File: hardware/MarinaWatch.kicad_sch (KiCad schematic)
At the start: 18 parts, among them J1 USB_C_Receptacle_USB2.0_16P, J2 Screw_Terminal_01x02, U1 ESP32-S3-MINI-1, U2 MCP73831-2-OT, U3 AP2112K-3.3

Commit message: Working on analog sensor
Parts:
- added Q101: PMOS, symbol Simulation_SPICE:PMOS
- added R101, R103: 110R, Resistor_SMD:R_0603_1608Metric_Pad0.98x0.95mm_HandSolder, symbol Device:R
- added R102: 100R, Resistor_SMD:R_0603_1608Metric_Pad0.98x0.95mm_HandSolder, symbol Device:R
- added TH101: 100R, symbol Device:Thermistor_PTC
- added TP101, TP102, TP103, TP104: TestPoint, symbol Connector:TestPoint
- added U101, U102, U103: ${SIM.PARAMS}, symbol Simulation_SPICE:OPAMP
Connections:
- net +3V3: now also R101.1, R103.1, U101.3 (V+), U102.3 (V+), U103.3 (V+)
- net GND: now also R102.2, TH101.2, U101.4 (V-), U102.4 (V-), U103.4 (V-)
- new net PT_ANALOG: R103.2, TH101.1, TP101.1, U101.1 (+)
- new net PT_DIFF_N: TP104.1, U102.2 (-), U102.5, U103.2 (-)
- new net PT_DIFF_P: TP103.1, U101.2 (-), U101.5, U103.1 (+)
- new net PT_REF: R101.2, R102.1, TP102.1, U102.1 (+)

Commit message: Working on production version
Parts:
- removed D1, D2, D3: 1N5819, Diode_SMD:D_SOD-123, symbol Diode:1N5819
- removed J2: Screw_Terminal_01x02, TerminalBlock_MetzConnect:TerminalBlock_MetzConnect_Type101_RT01602HBWC_1x02_P5.08mm_Horizontal, symbol Connector:Screw_Terminal_01x02
- removed Q101: PMOS, symbol Simulation_SPICE:PMOS
- removed R101, R103: 110R, Resistor_SMD:R_0603_1608Metric_Pad0.98x0.95mm_HandSolder, symbol Device:R
- removed R102: 100R, Resistor_SMD:R_0603_1608Metric_Pad0.98x0.95mm_HandSolder, symbol Device:R
- removed TH101: 100R, symbol Device:Thermistor_PTC
- removed TP101, TP102, TP103, TP104: TestPoint, symbol Connector:TestPoint
- removed U101, U102, U103: ${SIM.PARAMS}, symbol Simulation_SPICE:OPAMP
- removed U2: MCP73831-2-OT, Package_TO_SOT_SMD:SOT-23-5, symbol Battery_Management:MCP73831-2-OT
- removed U3: AP2112K-3.3, Package_TO_SOT_SMD:SOT-23-5, symbol Regulator_Linear:AP2112K-3.3
- added BT1, BT2: Battery_Cell, symbol Device:Battery_Cell
- added C3, C6: 10u, Capacitor_SMD:C_0603_1608Metric_Pad1.08x0.95mm_HandSolder, symbol Device:C
- added C4, C7, C8: 22u, Capacitor_SMD:C_0603_1608Metric_Pad1.08x0.95mm_HandSolder, symbol Device:C
- added C5: 100n, Capacitor_SMD:C_0603_1608Metric_Pad1.08x0.95mm_HandSolder, symbol Device:C
- added L1: 1u5, symbol Device:L
- added R10, R11, R12, R15, R9: 5k1, Resistor_SMD:R_0603_1608Metric_Pad0.98x0.95mm_HandSolder, symbol Device:R
- added R13: 470k, Resistor_SMD:R_0603_1608Metric_Pad0.98x0.95mm_HandSolder, symbol Device:R
- added R14: 150k, Resistor_SMD:R_0603_1608Metric_Pad0.98x0.95mm_HandSolder, symbol Device:R
- added TH1, TH2: Thermistor_NTC, symbol Device:Thermistor_NTC
- added U2, U4: BQ24210, symbol KiCAD-LIB:BQ24210
- added U5: TPS63070, symbol KiCAD-LIB:TPS63070
- R1, R2: value 12k -> 0R
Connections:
- net +3V3: now also C4.1, C7.1, C8.1, R13.1, U5.7 (VOUT), U5.8 (VOUT); no longer C2.1
- net +BATT: now also C2.1, R1.2, R2.2, BT1.1 (+), BT2.1 (+), C6.1, R15.1, U5.12 (VIN), U5.13 (VIN); no longer R5.1
- net GND: now also R7.2, BT1.2 (-), BT2.2 (-), C3.2, C4.2, C5.2, C6.2, C7.2, C8.2, R10.2, R11.2, R14.2, R9.2, TH1.2, TH2.2, U2.3 (VSS), U4.3 (VSS), U5.10 (PGND), U5.15 (VSEL), U5.4 (GND), U5.6 (FB2); no longer R2.2
- net SOLAR: now also C1.1, U2.1 (VBUS); no longer R7.1
- net VBUS: now also C3.1, U4.1 (VBUS)
- net V_BAT: no longer R5.2, R6.1
- net V_SOLAR: no longer R7.2, R8.1
- net at R2.1: now also U2.10 (BAT)
- net VCC: no longer names the net of R1.1
- net VCC: now also U4.10 (BAT); no longer C1.1
- new net: R12.1, U4.4 (VTSB)
- new net: R12.2, TH1.1, U4.5 (TS)
- new net: R13.2, R14.1, U5.5 (FB)
- new net: R5.1, U2.4 (VTSB)
- new net: R5.2, TH2.1, U2.5 (TS)
- new net: R10.1, U4.2 (ISET)
- new net: R9.1, U4.7 (~{EN})
- new net: R11.1, U4.9 (VDPM)
- new net: L1.1, U5.11 (L1)
- new net: L1.2, U5.9 (L2)
- new net: C5.1, U5.3 (VAUX)
- new net: R7.1, U2.2 (ISET)
- new net: R6.1, U2.7 (~{EN})
- new net: R8.1, U2.9 (VDPM)
- new net: R15.2, U5.1 (PS/SYNC), U5.14 (EN)
- no-connect marks 37 -> 41
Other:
- note added: "BATTERY CIRCUITRY"
- note removed: "BATTERY CHARGER"
- note removed: "POWER SUPPLY"
- note removed: "VOLTAGE MEASURMENTRS"
- moved on the sheet: J1, R3, R4, U1

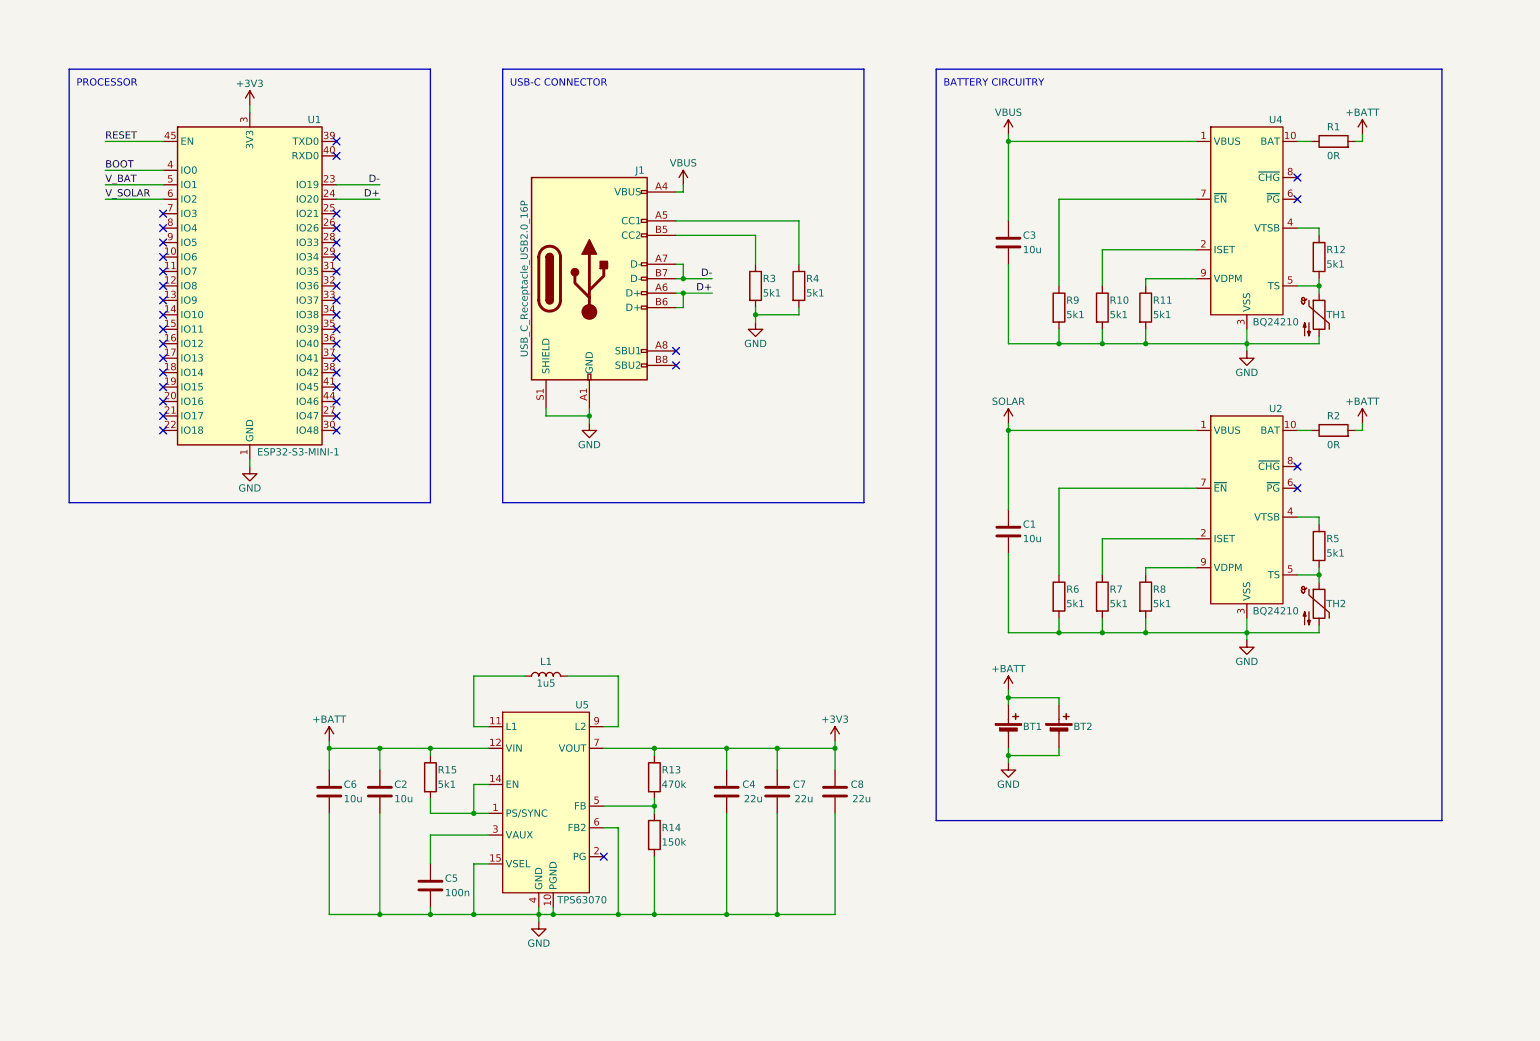
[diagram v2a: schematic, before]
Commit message: Added wheatstone bridge, battery chargers and 3v3 power supply
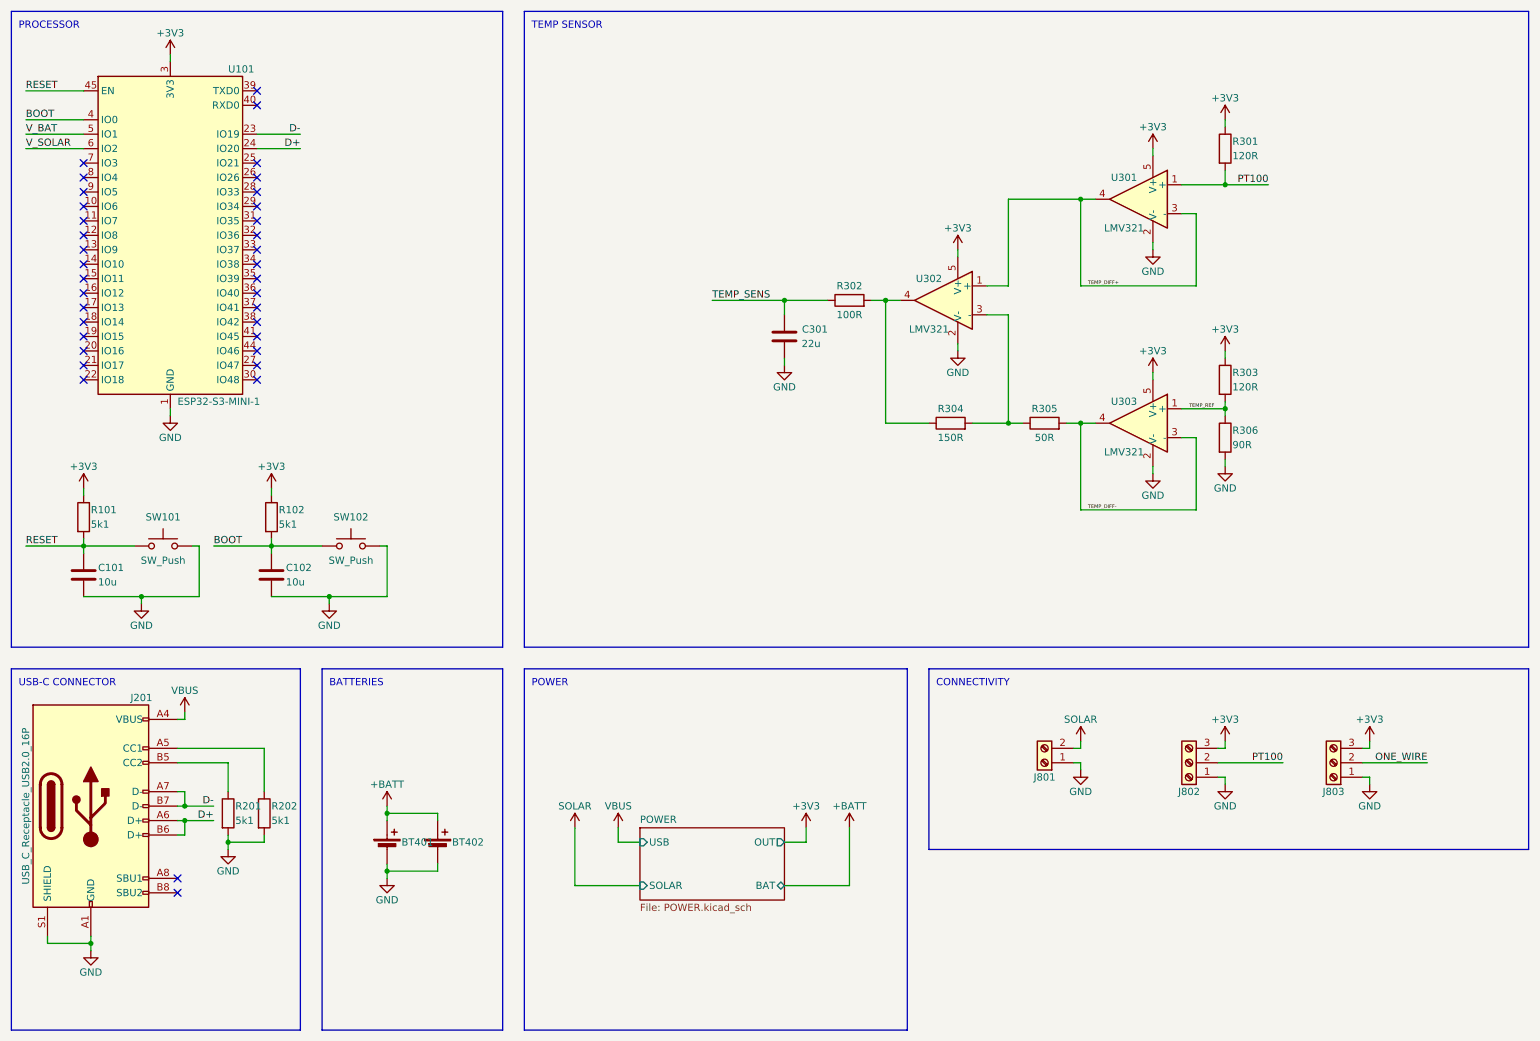
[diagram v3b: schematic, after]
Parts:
- removed C1, C2, C3, C6: 10u, Capacitor_SMD:C_0603_1608Metric_Pad1.08x0.95mm_HandSolder, symbol Device:C
- removed C4, C7, C8: 22u, Capacitor_SMD:C_0603_1608Metric_Pad1.08x0.95mm_HandSolder, symbol Device:C
- removed C5: 100n, Capacitor_SMD:C_0603_1608Metric_Pad1.08x0.95mm_HandSolder, symbol Device:C
- removed L1: 1u5, symbol Device:L
- removed R1, R2: 0R, Resistor_SMD:R_0603_1608Metric_Pad0.98x0.95mm_HandSolder, symbol Device:R
- removed R10, R11, R12, R15, R5, R6, R7, R8, R9: 5k1, Resistor_SMD:R_0603_1608Metric_Pad0.98x0.95mm_HandSolder, symbol Device:R
- removed R13: 470k, Resistor_SMD:R_0603_1608Metric_Pad0.98x0.95mm_HandSolder, symbol Device:R
- removed R14: 150k, Resistor_SMD:R_0603_1608Metric_Pad0.98x0.95mm_HandSolder, symbol Device:R
- removed TH1, TH2: Thermistor_NTC, symbol Device:Thermistor_NTC
- removed U2, U4: BQ24210, symbol KiCAD-LIB:BQ24210
- removed U5: TPS63070, symbol KiCAD-LIB:TPS63070
- added C101, C102: 10u, Capacitor_SMD:C_0603_1608Metric_Pad1.08x0.95mm_HandSolder, symbol Device:C
- added C301: 22u, Capacitor_SMD:C_0603_1608Metric_Pad1.08x0.95mm_HandSolder, symbol Device:C
- added J801: Screw_Terminal_01x02, symbol Connector:Screw_Terminal_01x02
- added J802, J803: Screw_Terminal_01x03, symbol Connector:Screw_Terminal_01x03
- added R101, R102: 5k1, Resistor_SMD:R_0603_1608Metric_Pad0.98x0.95mm_HandSolder, symbol Device:R
- added R301, R303: 120R, Resistor_SMD:R_0603_1608Metric_Pad0.98x0.95mm_HandSolder, symbol Device:R
- added R302: 100R, Resistor_SMD:R_0603_1608Metric_Pad0.98x0.95mm_HandSolder, symbol Device:R
- added R304: 150R, Resistor_SMD:R_0603_1608Metric_Pad0.98x0.95mm_HandSolder, symbol Device:R
- added R305: 50R, Resistor_SMD:R_0603_1608Metric_Pad0.98x0.95mm_HandSolder, symbol Device:R
- added R306: 90R, Resistor_SMD:R_0603_1608Metric_Pad0.98x0.95mm_HandSolder, symbol Device:R
- added SW101, SW102: SW_Push, symbol Switch:SW_Push
- added U301, U302, U303: LMV321, Package_TO_SOT_SMD:SOT-23-5, symbol Amplifier_Operational:LMV321
- renumbered BT1 to BT401, BT2 to BT402, J1 to J201, R3 to R201, R4 to R202, U1 to U101
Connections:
- net +3V3: now also J802.3 (Pin_3), J803.3 (Pin_3), R101.1, R102.1, R301.1, R303.1, U301.5 (V+), U302.5 (V+), U303.5 (V+)
- net BOOT: now also C102.1, R102.2, SW102.1
- net GND: now also C101.2, C102.2, C301.2, J801.1 (Pin_1), J802.1 (Pin_1), J803.1 (Pin_1), R306.2, SW101.2, SW102.2, U301.2 (V-), U302.2 (V-), U303.2 (V-)
- net RESET: now also C101.1, R101.2, SW101.1
- net SOLAR: now also J801.2 (Pin_2)
- new net: R302.2, R304.1, U302.4
- new net: R304.2, R305.1, U302.3 (-)
- new net ONE_WIRE: J803.2 (Pin_2)
- new net PT100: J802.2 (Pin_2), R301.2, U301.1 (+)
- new net TEMP_DIFF+: U301.3 (-), U301.4, U302.1 (+)
- new net TEMP_DIFF-: R305.2, U303.3 (-), U303.4
- new net TEMP_REF: R303.2, R306.1, U303.1 (+)
- new net TEMP_SENS: C301.1, R302.1
- no-connect marks 41 -> 36
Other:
- added sheet POWER (POWER.kicad_sch)
- note added: "BATTERIES"
- note added: "CONNECTIVITY"
- note added: "POWER"
- note added: "TEMP SENSOR"
- note removed: "BATTERY CIRCUITRY"
- company: (none) -> Alfred Wrigfors
- title: (none) -> MarinaWatch
- moved on the sheet: BT401, BT402, J201, R201, R202, U101

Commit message: Started with footprints and layout
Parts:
- added J401: Screw_Terminal_01x04, TerminalBlock:TerminalBlock_bornier-4_P5.08mm, symbol Connector:Screw_Terminal_01x04
- added R302: 200R, Resistor_SMD:R_0603_1608Metric_Pad0.98x0.95mm_HandSolder, symbol Device:R
- added R303: 90R, Resistor_SMD:R_0603_1608Metric_Pad0.98x0.95mm_HandSolder, symbol Device:R
- added R304: 1k5, Resistor_SMD:R_0603_1608Metric_Pad0.98x0.95mm_HandSolder, symbol Device:R
- added R901, R902: 3k, Resistor_SMD:R_0603_1608Metric_Pad0.98x0.95mm_HandSolder, symbol Device:R
- added R903, R904: 7k5, Resistor_SMD:R_0603_1608Metric_Pad0.98x0.95mm_HandSolder, symbol Device:R
- BT401, BT402: footprint (none) -> AlfredLib:18650
- J801: footprint (none) -> TerminalBlock:TerminalBlock_bornier-2_P5.08mm
- J802, J803: footprint (none) -> TerminalBlock:TerminalBlock_bornier-3_P5.08mm
- R307: renamed from R304; value 150R -> 1k5
- R308: renamed from R305; value 50R -> 200R
- renumbered R302 to R305, R303 to R306, R306 to R309
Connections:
- net V_BAT is gone; now on net TEMP_SENS: U101.5 (IO1)
- net +3V3: now also J401.4 (Pin_4)
- net +BATT: now also R901.1
- net GND: now also J401.1 (Pin_1), R303.2, R304.1, R903.2, R904.2
- net ONE_WIRE: now also U101.14 (IO10)
- net PT100: now also R303.1
- net SOLAR: now also R902.1
- net TEMP_DIFF+: now also R302.2, R304.2; no longer U302.1 (+)
- net I2C_SDA: now reaches U101.12 (IO8)
- net I2C_SDA: now also J401.3 (Pin_3)
- net I2C_SCL: now reaches U101.13 (IO9)
- net I2C_SCL: now also J401.2 (Pin_2)
- net SOLAR_SENSE: now reaches U101.7 (IO3)
- net SOLAR_SENSE: now also R902.2, R904.1
- net AMP_OUT: now reaches R305.2, R307.1, U302.4
- net AMP-: now reaches R307.2, R308.1, U302.3 (-)
- net V_SOLAR renamed BAT_SENSE
- net BAT_SENSE: now also R901.2, R903.1
- new net AMP+: R302.1, U302.1 (+)
- no-connect marks 36 -> 31
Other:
- note added: "G = 1500 / 200 = 7.5"
- moved on the sheet: BT401, J801, J802, J803, R301, R306, R307, R308, R309, U101, U301, U303

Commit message: Working on power circuitry layout
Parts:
- removed J803: Screw_Terminal_01x03, TerminalBlock:TerminalBlock_bornier-3_P5.08mm, symbol Connector:Screw_Terminal_01x03
- added R801, R802: 100R, Resistor_SMD:R_0603_1608Metric_Pad0.98x0.95mm_HandSolder, symbol Device:R
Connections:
- net ONE_WIRE: now also R802.2
- net PT100: now also R801.2; no longer J802.2 (Pin_2)
- new net SIG: J802.2 (Pin_2), R801.1, R802.1
